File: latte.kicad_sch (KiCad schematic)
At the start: 76 parts, among them J1 SOIC bite, J2 USB_C_Receptacle_USB2.0, J3 USB_C_Receptacle_USB2.0, J4 USB_C_2.0, J5 USB_A, J6 OUT1, J8 SENSE1, Q1 IRLML0030, SW1 USB BOOT, U1 RP2040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

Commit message: Diff pair routing done
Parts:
- removed D13: BAV99, Package_TO_SOT_SMD:SOT-23, symbol Diode:BAV99
- removed J8: SENSE1, TerminalBlock:TerminalBlock_bornier-2_P5.08mm, symbol Connector_Generic:Conn_01x02
- removed R27: 10k, Resistor_SMD:R_0603_1608Metric, symbol Device:R
- removed R29: DNP, Resistor_SMD:R_0603_1608Metric, symbol Device:R
- added C20: 100n, Capacitor_SMD:C_0603_1608Metric, symbol Device:C
- added D11, D12, D15, D16, D17, D4: BAV99, Package_TO_SOT_SMD:SOT-23, symbol Diode:BAV99
- added J7: SMART PROBE, Connector_RJ:RJ45_Amphenol_54602-x08_Horizontal, symbol Connector:RJ45
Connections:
- net +3V3: now also C20.1, D11.2 (A), D12.2 (A), D15.2 (A), D16.2 (A), D17.2 (A), D4.2 (A), J7.1
- net DUT_USB_D+: now also U1.16 (GPIO13)
- net DUT_USB_D-: now also U1.15 (GPIO12)
- net GND: now also C20.2, D11.1 (K), D12.1 (K), D15.1 (K), D16.1 (K), D17.1 (K), D4.1 (K), J7.8
- net DUT_USBA_D+: now reaches U6.1 (HSD1+), U8.1 (I/O1)
- net DUT_USBC_D+: now reaches U6.2 (HSD2+), U7.4 (I/O2)
- net DUT_USBC_D-: now reaches U6.6 (HSD2-), U7.6 (I/O1)
- net DUT_USBA_D-: now reaches U6.7 (HSD1-), U8.3 (I/O2)
- net SMART_SDA: now reaches U1.4 (GPIO2)
- net SMART_SDA: now also D17.3 (K), J7.2
- net D-: now reaches R9.2, U1.46 (USB_DM)
- net D+: now reaches R8.2, U1.47 (USB_DP)
- net SMART_SCL: now reaches U1.5 (GPIO3)
- net SMART_SCL: now also D16.3 (K), J7.3
- net SMART_MISC1: now reaches U1.6 (GPIO4)
- net SMART_MISC1: now also D15.3 (K), J7.4
- net SMART_MISC2: now reaches U1.7 (GPIO5)
- net SMART_MISC2: now also D12.3 (K), J7.5
- net SMART_MISC3: now reaches U1.8 (GPIO6)
- net SMART_MISC3: now also D11.3 (K), J7.6
- net SMART_SENSE: now reaches U1.9 (GPIO7)
- net SMART_SENSE: now also D4.3 (K), J7.7
- net USBA_D-: now reaches J5.2 (D-), U8.4 (I/O2)
- net USBA_D+: now reaches J5.3 (D+), U8.6 (I/O1)
- no-connect marks 31 -> 20
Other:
- note added: "Pins 15 and 16 used just for simpler routing"
- moved on the sheet: C1, C18, C19, C2, C3, D1, D10, D14, D2, D3, D5, D6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

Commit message: Routing done
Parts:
- removed C20: 100n, Capacitor_SMD:C_0603_1608Metric, symbol Device:C
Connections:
- net SENSE2 is gone; now on net SMART_SENSE: U1.39 (GPIO27_ADC1)
- net SMART_SENSE: no longer U1.9 (GPIO7)
- net at U1.17 (GPIO14): no longer D7.2 (A)
- net at U1.18 (GPIO15): no longer D8.2 (A)
- net at U1.27 (GPIO16): no longer D9.2 (A)
- net at U1.29 (GPIO18): now also D9.2 (A)
- net at U1.30 (GPIO19): now also D8.2 (A)
- net at U1.31 (GPIO20): now also D7.2 (A)
- net OUT2: no longer names the net of U1.3 (GPIO1)
- net SENSE1: no longer names the net of U1.38 (GPIO26_ADC0)
- no-connect marks 20 -> 26
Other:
- moved on the sheet: D7, D8, D9, R17, R18, R19

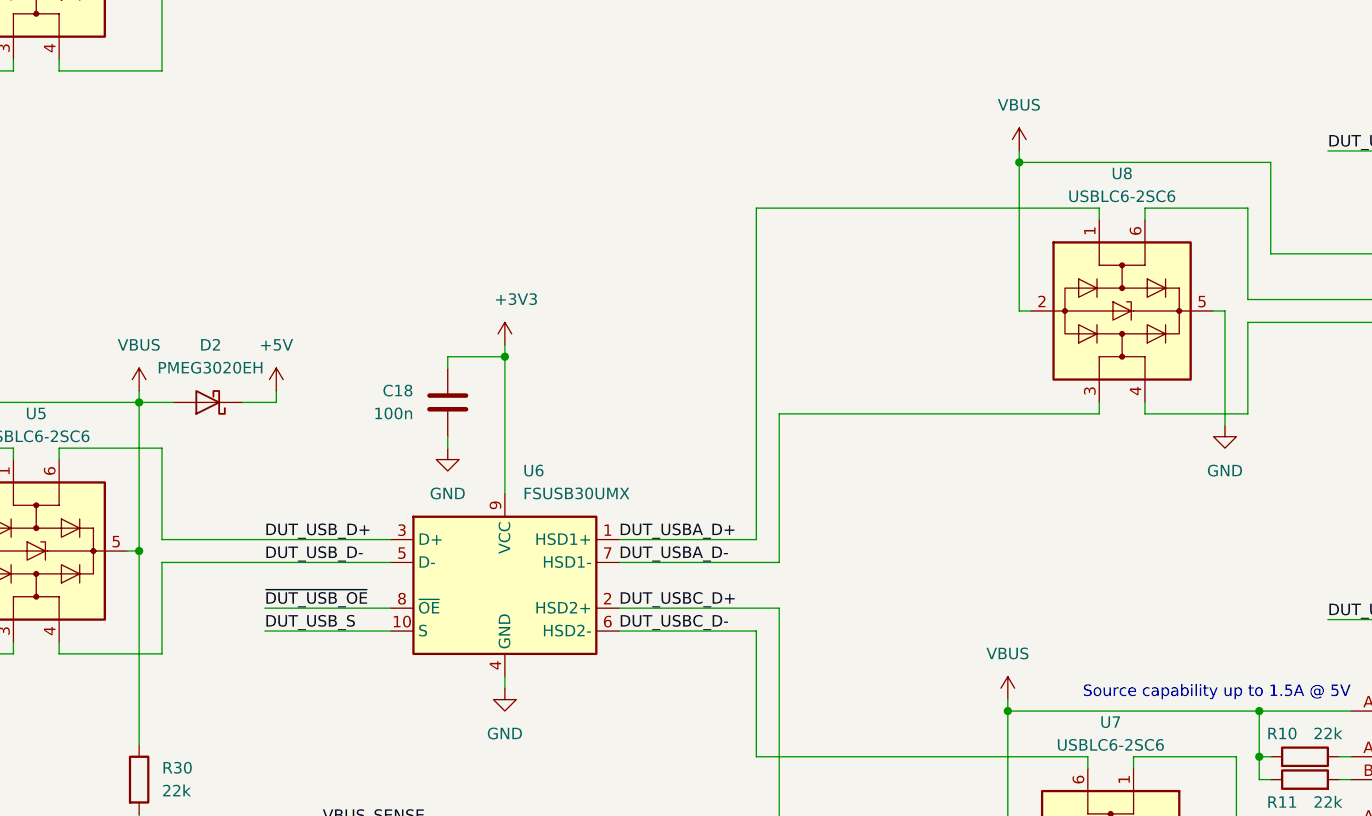
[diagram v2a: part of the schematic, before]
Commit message: Fixed switched D+/D- on PC DUT USB connector
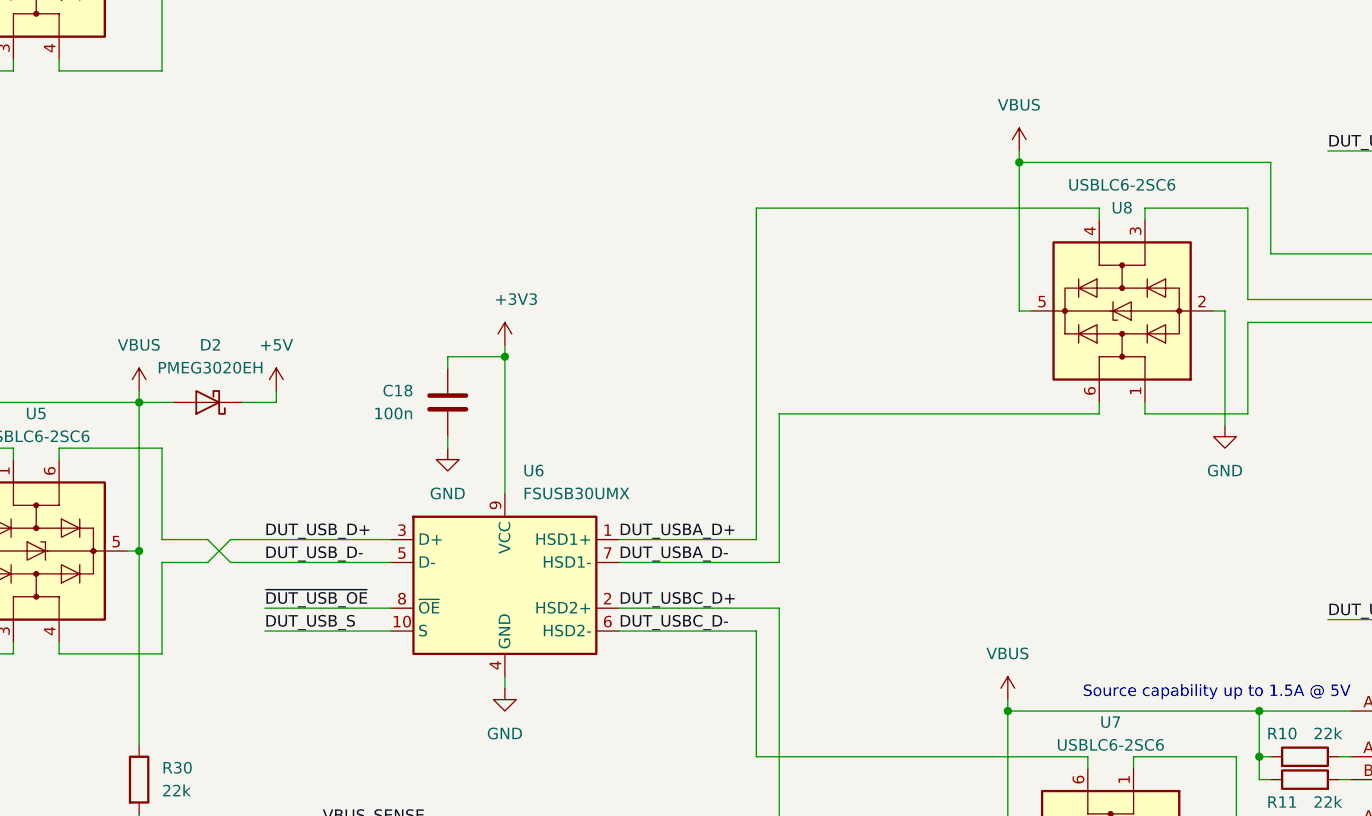
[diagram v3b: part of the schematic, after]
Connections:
- net DUT_USBA_D+: now also U8.4 (I/O2); no longer U8.1 (I/O1)
- net DUT_USBA_D-: now also U8.6 (I/O1); no longer U8.3 (I/O2)
- net DUT_USB_D+: now also U5.4 (I/O2); no longer U5.6 (I/O1)
- net DUT_USB_D-: now also U5.6 (I/O1); no longer U5.4 (I/O2)
- net GND: now also U8.2 (GND); no longer U8.5 (VBUS)
- net USBA_D+: now also U8.3 (I/O2); no longer U8.6 (I/O1)
- net USBA_D-: now also U8.1 (I/O1); no longer U8.4 (I/O2)
- net VBUS: now also U8.5 (VBUS); no longer U8.2 (GND)
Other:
- moved on the sheet: U8
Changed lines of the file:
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@@
-    (stroke (width 0) (type default) (color 0 0 0 0))
-  )
-  (wire (pts (xy 100.33 220.98) (xy 125.73 220.98))
     (stroke (width 0) (type default) (color 0 0 0 0))
   )
@@
     (stroke (width 0) (type default) (color 0 0 0 0))
   )
+  (wire (pts (xy 107.95 220.98) (xy 125.73 220.98))
+    (stroke (width 0) (type default) (color 0 0 0 0))
+  )
   (wire (pts (xy 261.62 227.33) (xy 261.62 228.6))
     (stroke (width 0) (type default) (color 0 0 0 0))
@@
     (stroke (width 0) (type default) (color 0 0 0 0))
   )
+  (wire (pts (xy 105.41 220.98) (xy 107.95 218.44))
+    (stroke (width 0) (type default) (color 0 0 0 0))
+  )
   (wire (pts (xy 232.41 252.73) (xy 231.14 252.73))
     (stroke (width 0) (type default) (color 0 0 0 0))
@@
     (stroke (width 0) (type default) (color 0 0 0 0))
   )
-  (wire (pts (xy 125.73 218.44) (xy 100.33 218.44))
-    (stroke (width 0) (type default) (color 0 0 0 0))
-  )
   (wire (pts (xy 297.18 149.86) (xy 297.18 157.48))
     (stroke (width 0) (type default) (color 0 0 0 0))
@@
     (stroke (width 0) (type default) (color 0 0 0 0))
   )
+  (wire (pts (xy 107.95 218.44) (xy 125.73 218.44))
+    (stroke (width 0) (type default) (color 0 0 0 0))
+  )
   (wire (pts (xy 299.72 179.07) (xy 299.72 177.8))
     (stroke (width 0) (type default) (color 0 0 0 0))
@@
     (stroke (width 0) (type default) (color 0 0 0 0))
   )
-  (wire (pts (xy 100.33 220.98) (xy 100.33 231.14))
-    (stroke (width 0) (type default) (color 0 0 0 0))
-  )
   (wire (pts (xy 30.48 29.21) (xy 30.48 27.94))
     (stroke (width 0) (type default) (color 0 0 0 0))
@@
     (stroke (width 0) (type default) (color 0 0 0 0))
   )
+  (wire (pts (xy 97.79 219.71) (xy 97.79 241.3))
+    (stroke (width 0) (type default) (color 0 0 0 0))
+  )
+  (wire (pts (xy 100.33 218.44) (xy 105.41 218.44))
+    (stroke (width 0) (type default) (color 0 0 0 0))
+  )
   (wire (pts (xy 163.83 48.26) (xy 184.15 48.26))
     (stroke (width 0) (type default) (color 0 0 0 0))
@@
     (stroke (width 0) (type default) (color 0 0 0 0))
   )
+  (wire (pts (xy 100.33 220.98) (xy 105.41 220.98))
+    (stroke (width 0) (type default) (color 0 0 0 0))
+  )
   (wire (pts (xy 88.9 209.55) (xy 88.9 208.28))
     (stroke (width 0) (type default) (color 0 0 0 0))
@@
     (stroke (width 0) (type default) (color 0 0 0 0))
   )
-  (wire (pts (xy 97.79 219.71) (xy 97.79 241.3))
-    (stroke (width 0) (type default) (color 0 0 0 0))
-  )
   (wire (pts (xy 247.65 38.1) (xy 259.08 38.1))
     (stroke (width 0) (type default) (color 0 0 0 0))
@@
     (stroke (width 0) (type default) (color 0 0 0 0))
   )
+  (wire (pts (xy 107.95 220.98) (xy 105.41 218.44))
+    (stroke (width 0) (type default) (color 0 0 0 0))
+  )
   (wire (pts (xy 220.98 191.77) (xy 245.11 191.77))
     (stroke (width 0) (type default) (color 0 0 0 0))
@@
   )
   (wire (pts (xy 281.94 38.1) (xy 293.37 38.1))
+    (stroke (width 0) (type default) (color 0 0 0 0))
+  )
+  (wire (pts (xy 100.33 231.14) (xy 100.33 220.98))
     (stroke (width 0) (type default) (color 0 0 0 0))
   )
@@
     (pin "1")
   )
-  (symbol (lib_id "Power_Protection:USBLC6-2SC6") (at 207.01 193.04 270) (unit 1)
+  (symbol (lib_id "Power_Protection:USBLC6-2SC6") (at 207.01 193.04 90) (unit 1)
     (in_bom yes) (on_board yes)
-    (property "Reference" "U8" (id 0) (at 207.01 177.8 90))
-    (property "Value" "USBLC6-2SC6" (id 1) (at 207.01 180.34 90))
-    (property "Footprint" "Package_TO_SOT_SMD:SOT-23-6" (id 2) (at 194.31 193.04 0)
-      (effects (font (size 1.27 1.27)) hide)
-    )
-    (property "Datasheet" "https://www.st.com/resource/en/datasheet/usblc6-2.pdf" (id 3) (at 215.9 198.12 0)
-      (effects (font (size 1.27 1.27)) hide)
-    )
+    (property "Reference" "U8" (id 0) (at 207.01 181.61 90))
+    (property "Value" "USBLC6-2SC6" (id 1) (at 207.01 179.07 90))
+    (property "Footprint" "Package_TO_SOT_SMD:SOT-23-6" (id 2) (at 219.71 193.04 0)
+      (effects (font (size 1.27 1.27)) hide)
+    )
+    (property "Datasheet" "https://www.st.com/resource/en/datasheet/usblc6-2.pdf" (id 3) (at 198.12 187.96 0)
+      (effects (font (size 1.27 1.27)) hide)
+    )
